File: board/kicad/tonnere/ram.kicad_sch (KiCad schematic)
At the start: 8 parts, among them U28 IS61WV204816BLL-10BLI, U32 IS61WV204816BLL-10BLI, U35 AS4C16M16SA

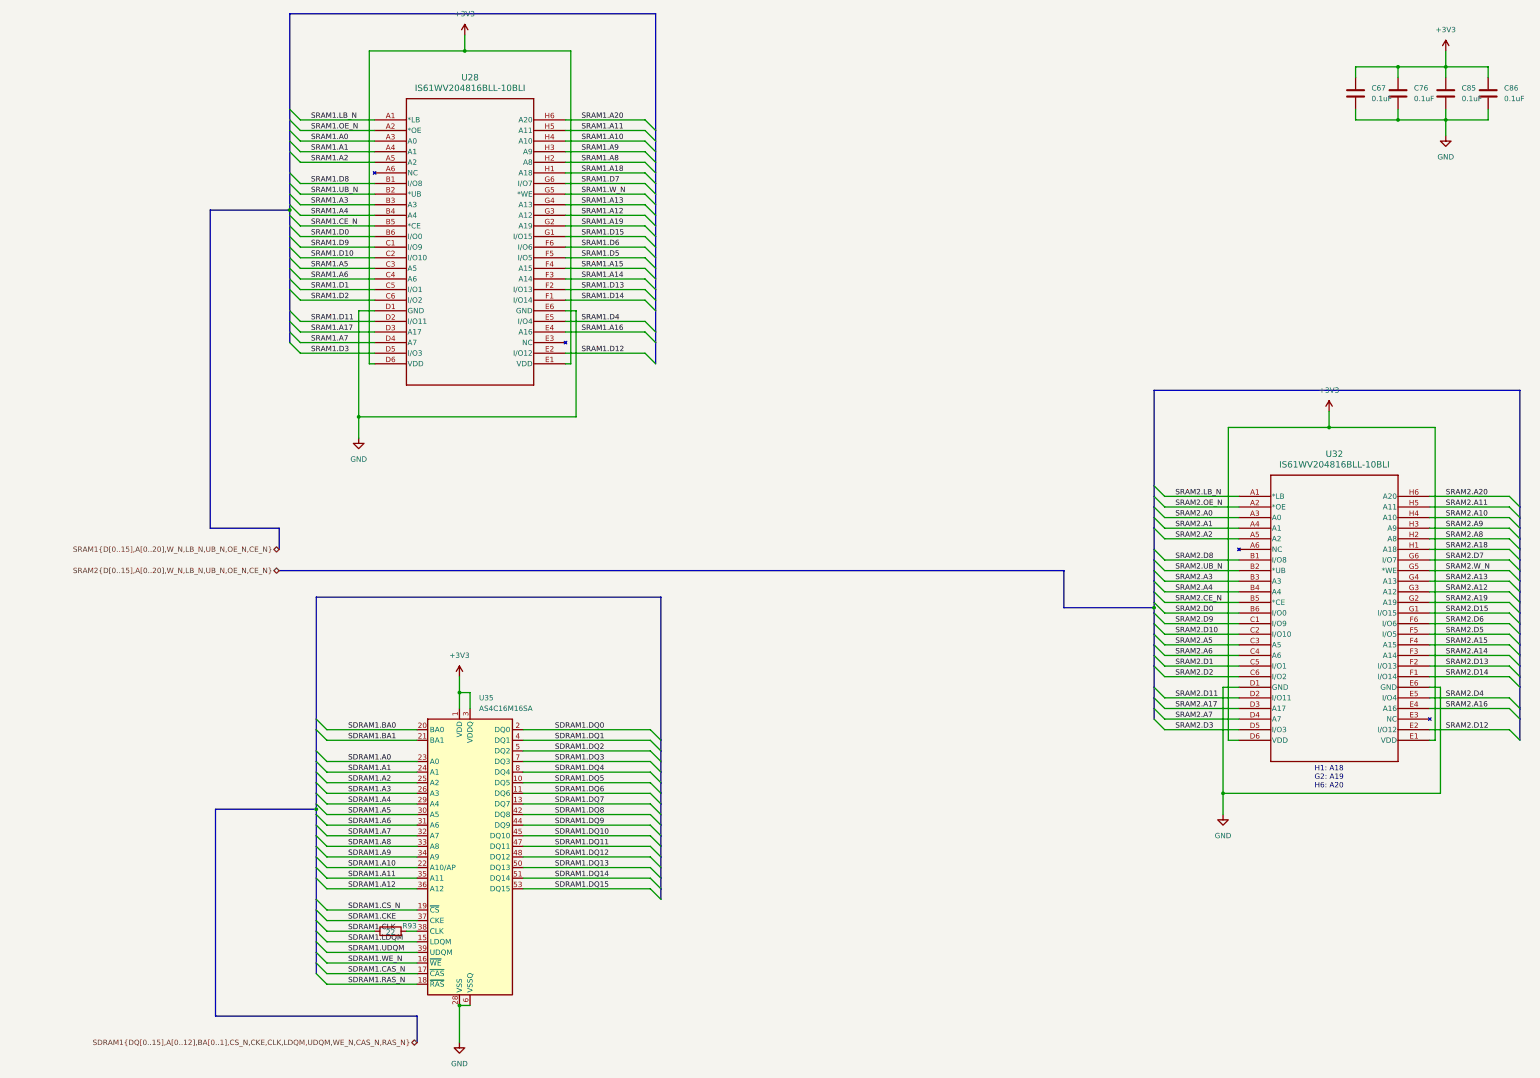
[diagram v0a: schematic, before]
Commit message: 0.60 (not final). Fix errata from 0.51. Added USB2 phy.
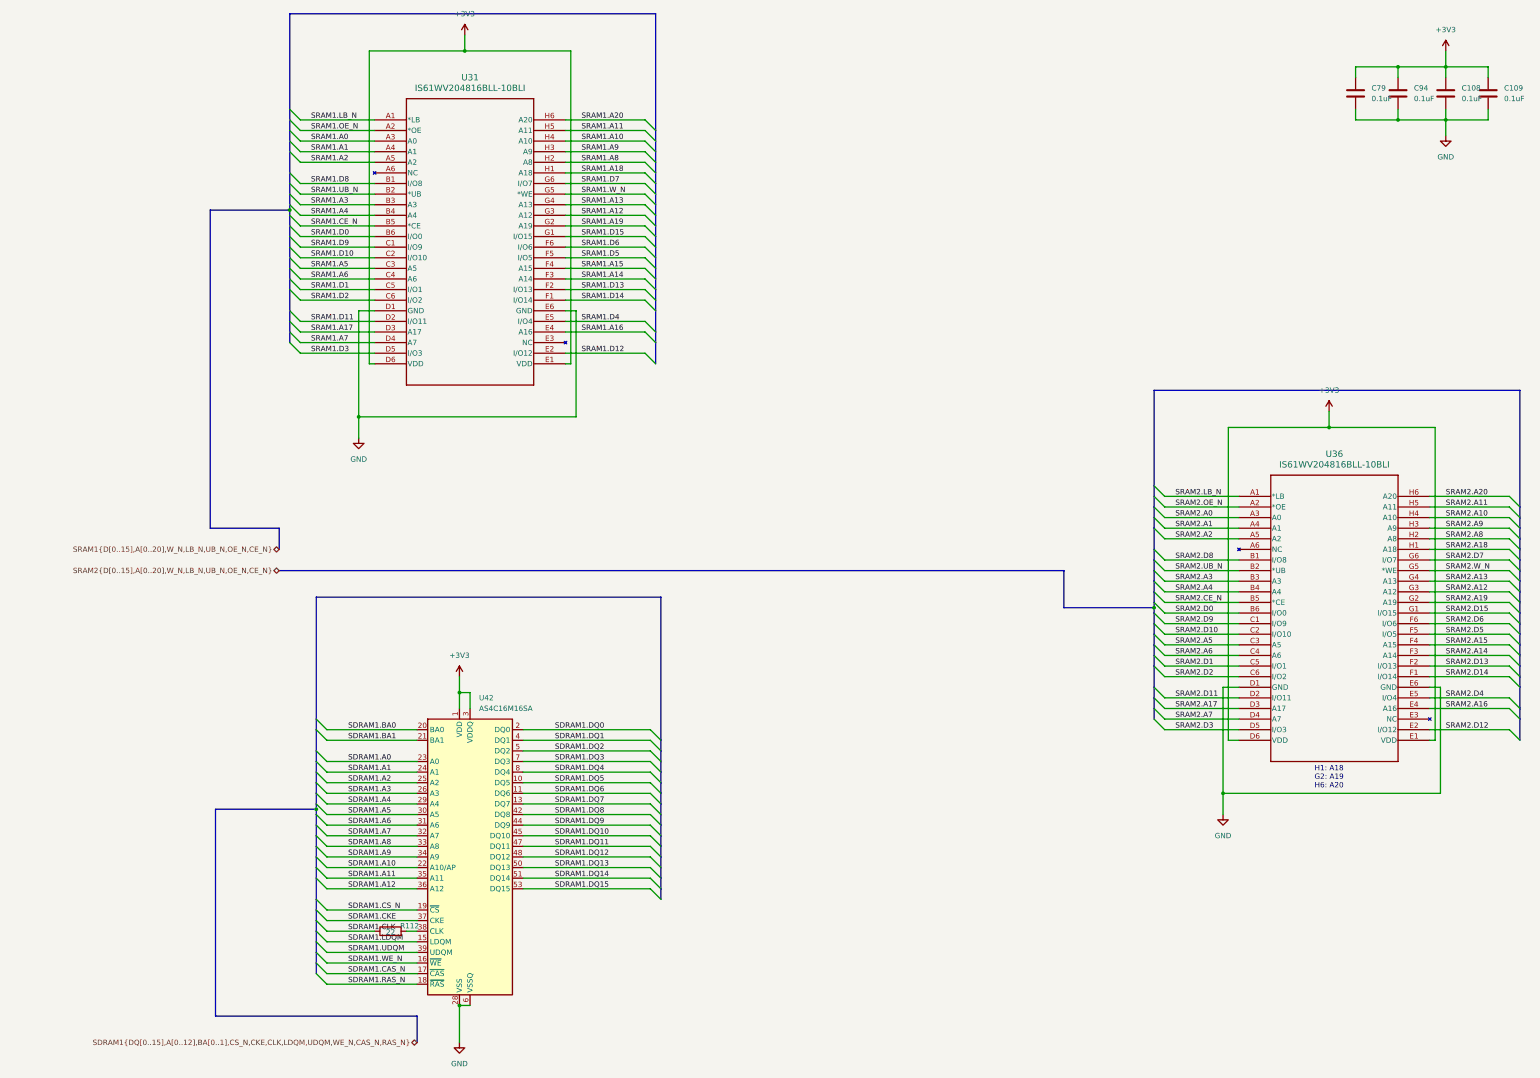
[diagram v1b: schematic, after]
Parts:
- renumbered C85 to C108, C86 to C109, C67 to C79, C76 to C94, R93 to R112, U28 to U31, U32 to U36, U35 to U42
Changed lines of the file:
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@@
 		(dnp no)
 		(fields_autoplaced yes)
-		(property "Reference" "C67"
+		(property "Reference" "C79"
 			(at 327.66 43.1799 0)
 			(effects
@@
 			(project "tonnere"
 				(path "/eb8e239c-f2ec-4b57-8f5c-6c75d6b59ab3/697ece47-2a2f-49f7-b3cd-8d11bcc6cfcf"
-					(reference "C67")
+					(reference "C79")
 					(unit 1)
 				)
@@
 		(dnp no)
 		(fields_autoplaced yes)
-		(property "Reference" "C86"
+		(property "Reference" "C109"
 			(at 359.41 43.1799 0)
 			(effects
@@
 			(project "tonnere"
 				(path "/eb8e239c-f2ec-4b57-8f5c-6c75d6b59ab3/697ece47-2a2f-49f7-b3cd-8d11bcc6cfcf"
-					(reference "C86")
+					(reference "C109")
 					(unit 1)
 				)
@@
 		(dnp no)
 		(fields_autoplaced yes)
-		(property "Reference" "U35"
+		(property "Reference" "U42"
 			(at 113.9033 189.23 0)
 			(effects
@@
 			(project "tonnere"
 				(path "/eb8e239c-f2ec-4b57-8f5c-6c75d6b59ab3/697ece47-2a2f-49f7-b3cd-8d11bcc6cfcf"
-					(reference "U35")
+					(reference "U42")
 					(unit 1)
 				)
@@
 		(dnp no)
 		(fields_autoplaced yes)
-		(property "Reference" "C85"
+		(property "Reference" "C108"
 			(at 349.25 43.1799 0)
 			(effects
@@
 			(project "tonnere"
 				(path "/eb8e239c-f2ec-4b57-8f5c-6c75d6b59ab3/697ece47-2a2f-49f7-b3cd-8d11bcc6cfcf"
-					(reference "C85")
+					(reference "C108")
 					(unit 1)
 				)
@@
 		(on_board yes)
 		(dnp no)
-		(property "Reference" "R93"
+		(property "Reference" "R112"
 			(at 97.282 243.84 90)
 			(effects
@@
 			(project "tonnere"
 				(path "/eb8e239c-f2ec-4b57-8f5c-6c75d6b59ab3/697ece47-2a2f-49f7-b3cd-8d11bcc6cfcf"
-					(reference "R93")
+					(reference "R112")
 					(unit 1)
 				)
@@
 		(dnp no)
 		(fields_autoplaced yes)
-		(property "Reference" "C76"
+		(property "Reference" "C94"
 			(at 337.82 43.1799 0)
 			(effects
@@
 			(project "tonnere"
 				(path "/eb8e239c-f2ec-4b57-8f5c-6c75d6b59ab3/697ece47-2a2f-49f7-b3cd-8d11bcc6cfcf"
-					(reference "C76")
+					(reference "C94")
 					(unit 1)
 				)
@@
 		(dnp no)
 		(fields_autoplaced yes)
-		(property "Reference" "U32"
+		(property "Reference" "U36"
 			(at 318.77 130.81 0)
 			(effects
@@
 			(project "tonnere"
 				(path "/eb8e239c-f2ec-4b57-8f5c-6c75d6b59ab3/697ece47-2a2f-49f7-b3cd-8d11bcc6cfcf"
-					(reference "U32")
+					(reference "U36")
 					(unit 1)
 				)
@@
 		(dnp no)
 		(fields_autoplaced yes)
-		(property "Reference" "U28"
+		(property "Reference" "U31"
 			(at 111.76 40.64 0)
 			(effects
@@
 			(project "tonnere"
 				(path "/eb8e239c-f2ec-4b57-8f5c-6c75d6b59ab3/697ece47-2a2f-49f7-b3cd-8d11bcc6cfcf"
-					(reference "U28")
-					(unit 1)
-				)
+					(reference "U31")
+					(unit 1)
+				)
